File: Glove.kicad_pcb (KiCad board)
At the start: 4 copper layers, 72.8 x 52 mm, 42 parts, among them J1 USB_C_Receptacle_USB2.0, J2 Joystick, Q1 2N7002, Q2 2N7002, U1 LM1117-3.3, U2 ESP32-WROOM-32D, U3 CP2102N-Axx-xQFN24

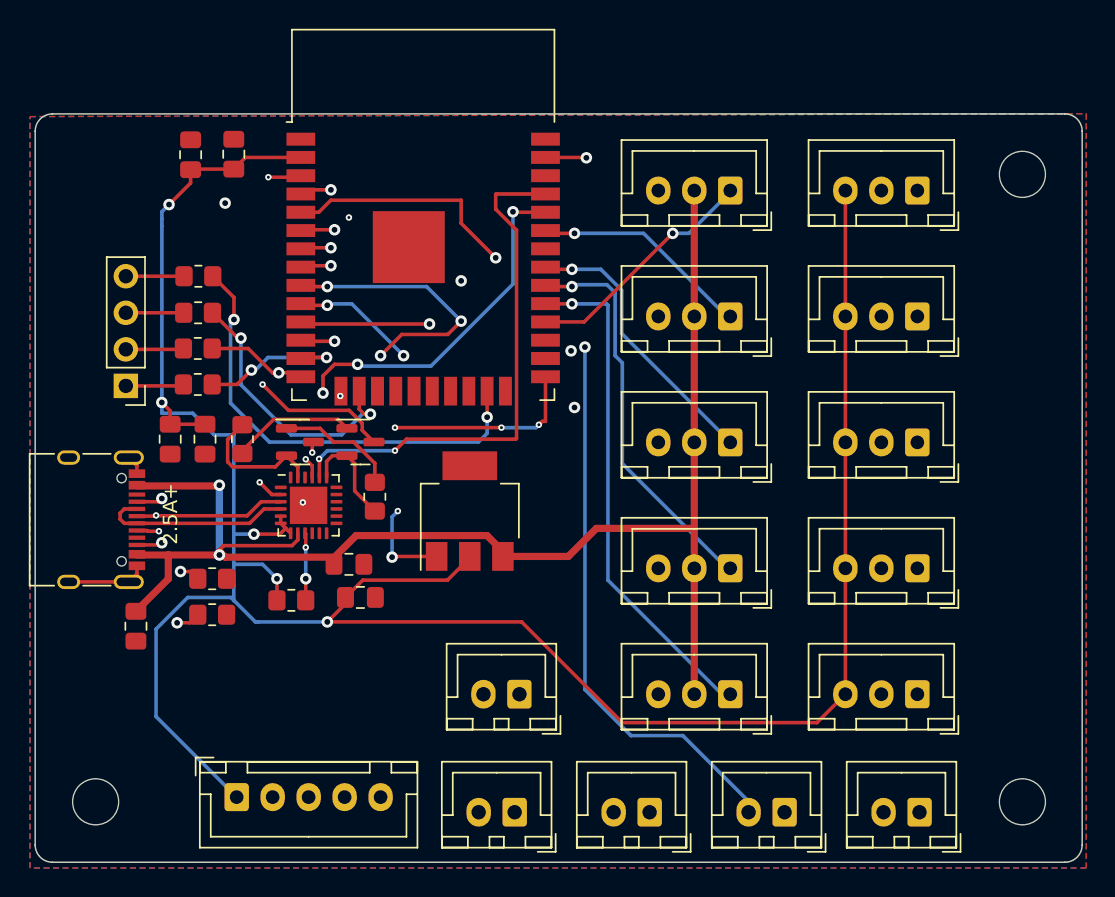
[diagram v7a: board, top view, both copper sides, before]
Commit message: Add 4th screw hole and branding
Signed-off-by: David Vogman <davidv@edgegaming.gg>
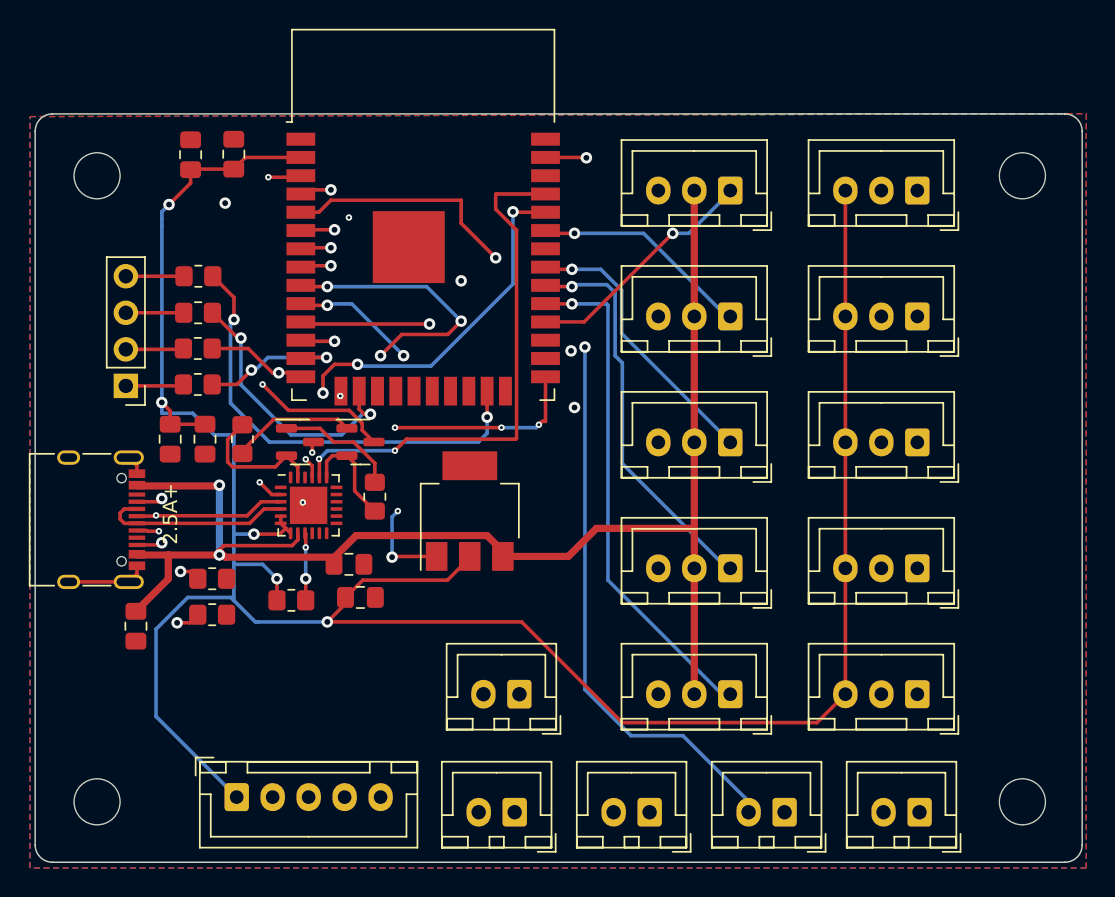
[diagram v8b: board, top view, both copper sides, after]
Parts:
- added REF**: MountingHole_3.2mm_M3, MountingHole:MountingHole_3.2mm_M3, F.Cu at (114.5, 60.5)
- moved REF** 0.10 mm to (178.8, 60.5)
- moved REF** 0.10 mm to (114.5, 104.0)
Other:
- board text added: "LucidVR PCB for Prototype 4 by Kozova1"
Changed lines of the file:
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@@
   (net 64 "Net-(R9-Pad2)")
   (footprint "MountingHole:MountingHole_3.2mm_M3" (layer "F.Cu")
-    (at 178.8 60.4)
+    (at 178.8 60.5)
     (descr "Mounting Hole 3.2mm, no annular, M3")
     (tags "mounting hole 3.2mm no annular m3")
@@
     )
   )
+  (footprint "MountingHole:MountingHole_3.2mm_M3" (layer "F.Cu")
+    (at 114.5 60.5)
+    (descr "Mounting Hole 3.2mm, no annular, M3")
+    (tags "mounting hole 3.2mm no annular m3")
+    (attr exclude_from_pos_files exclude_from_bom)
+    (fp_text reference "REF**" (at 0 -4.2) (layer "F.SilkS") hide
+      (effects (font (size 1 1) (thickness 0.15)))
+    )
+    (fp_text value "MountingHole_3.2mm_M3" (at 0 4.2) (layer "F.Fab")
+      (effects (font (size 1 1) (thickness 0.15)))
+    )
+    (fp_text user "${REFERENCE}" (at 0 0) (layer "F.Fab") hide
+      (effects (font (size 1 1) (thickness 0.15)))
+    )
+    (fp_circle (center 0 0) (end 3.2 0) (layer "Cmts.User") (width 0.15) (fill none))
+    (fp_circle (center 0 0) (end 3.45 0) (layer "F.CrtYd") (width 0.05) (fill none))
+    (pad "" np_thru_hole circle (at 0 0) (size 3.2 3.2) (drill 3.2) (layers *.Cu *.Mask))
+  )
   (footprint "Resistor_SMD:R_0805_2012Metric_Pad1.20x1.40mm_HandSolder" (layer "F.Cu")
     (at 121.5 72.5 180)
@@
   )
   (footprint "MountingHole:MountingHole_3.2mm_M3" (layer "F.Cu")
-    (at 114.4 104)
+    (at 114.5 104)
     (descr "Mounting Hole 3.2mm, no annular, M3")
     (tags "mounting hole 3.2mm no annular m3")
@@
     (effects (font (size 1 1) (thickness 0.15)) (justify mirror))
   )
+  (gr_text "LucidVR PCB\nfor Prototype 4\nby Kozova1" (at 137 59.5) (layer "B.SilkS")
+    (effects (font (size 1 1) (thickness 0.15)) (justify mirror))
+  )
